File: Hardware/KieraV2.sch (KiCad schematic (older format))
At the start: 32 parts, among them J1 Conn_01x04_Male, J2 Conn_01x05_Male, SW3 SW_Push, SW4 SW_MEC_5G, SW5 SW_Push, SW6 SW_Push, U1 STM32L4P5RET6, Y1 Crystal_GND24

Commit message: added button for starting procedure, changes to pcb layout pending
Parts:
- removed C3, C5, C6: 100nF, Capacitor_SMD:C_0603_1608Metric, symbol Device:C
- removed R12, R14, R16: 1k, Resistor_SMD:R_0603_1608Metric, symbol Device:R
- removed R13, R15, R17: 10k, Resistor_SMD:R_0603_1608Metric, symbol Device:R
- removed SW3, SW5, SW6: SW_Push, Button_Switch_THT:MyPushbuttonSwitch, symbol Switch:SW_Push
- renumbered SW4 to SW7
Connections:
- net SW3: now also U1.51 (PC10)
- net SW4: now also U1.52 (PC11)
- net SW5: now also U1.53 (PC12)
- net SW6: now reaches U1.54 (PD2)
- no-connect marks 30 -> 29

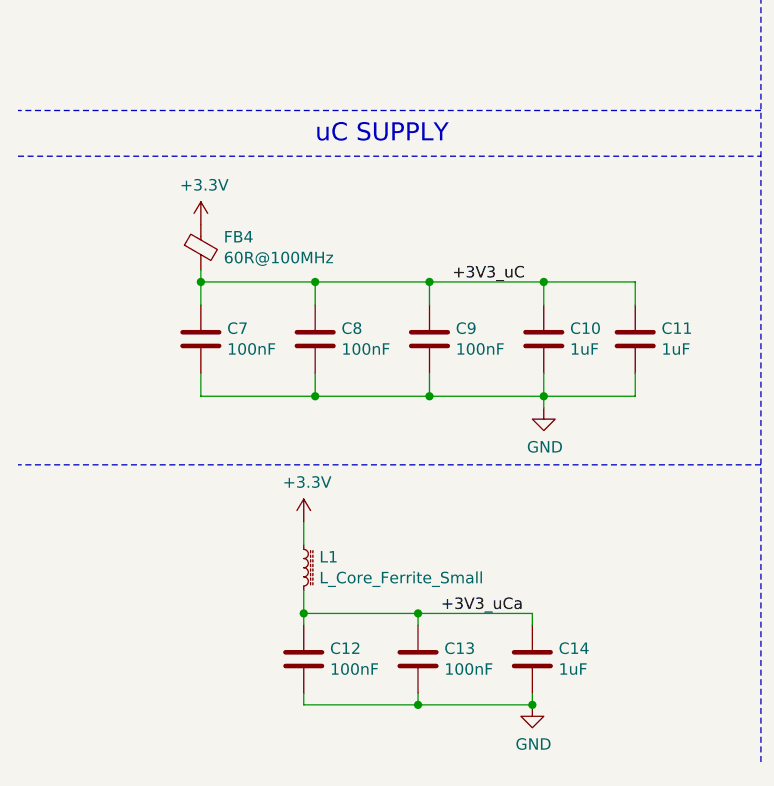
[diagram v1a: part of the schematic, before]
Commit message: controll leds are now groundend on uC, some changes of the pcb layout
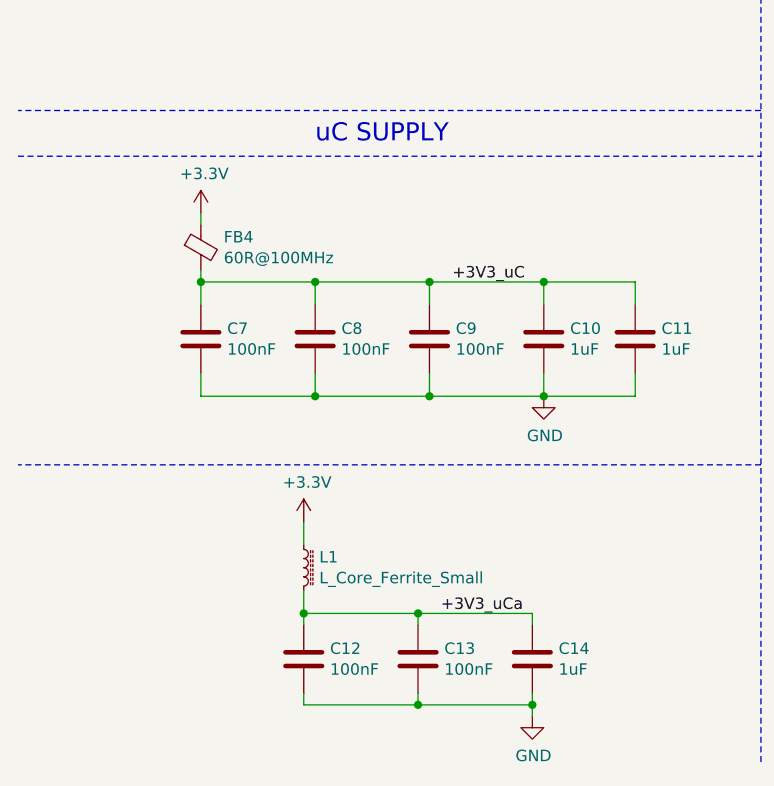
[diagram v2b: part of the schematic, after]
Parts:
- SW7: footprint Button_Switch_SMD:SW_Push_1P1T_NO_6x6mm_H9.5mm -> Button_Switch_SMD:SW_SPST_Omron_B3FS-100xP
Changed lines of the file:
@@
 	1    0    0    -1
 $EndComp
-$Comp
-L Device:C C7
-U 1 1 61B5E0FC
-P 1300 5900
-F 0 "C7" H 1415 5946 50  0000 L CNN
-F 1 "100nF" H 1415 5855 50  0000 L CNN
-F 2 "Capacitor_SMD:C_0603_1608Metric" H 1338 5750 50  0001 C CNN
-F 3 "~" H 1300 5900 50  0001 C CNN
-	1    1300 5900
-	1    0    0    -1
-$EndComp
-Wire Wire Line
-	1300 5650 1300 5750
-Wire Wire Line
-	1300 5650 1800 5650
-Wire Wire Line
-	1800 5650 1800 5750
-Wire Wire Line
-	1800 5650 2300 5650
-Wire Wire Line
-	2300 5650 2300 5750
-Connection ~ 1800 5650
-Wire Wire Line
-	2300 5650 2800 5650
-Connection ~ 2300 5650
-Wire Wire Line
-	1300 6050 1300 6150
 Wire Wire Line
 	1800 6050 1800 6150
@@
 L power:+3.3V #PWR014
 U 1 1 61B8345C
-P 1300 5400
-F 0 "#PWR014" H 1300 5250 50  0001 C CNN
-F 1 "+3.3V" H 1315 5573 50  0000 C CNN
-F 2 "" H 1300 5400 50  0001 C CNN
-F 3 "" H 1300 5400 50  0001 C CNN
-	1    1300 5400
+P 1300 5350
+F 0 "#PWR014" H 1300 5200 50  0001 C CNN
+F 1 "+3.3V" H 1315 5523 50  0000 C CNN
+F 2 "" H 1300 5350 50  0001 C CNN
+F 3 "" H 1300 5350 50  0001 C CNN
+	1    1300 5350
 	1    0    0    -1
 $EndComp
@@
 L power:GND #PWR017
 U 1 1 61B9E8D8
-P 2800 6200
-F 0 "#PWR017" H 2800 5950 50  0001 C CNN
-F 1 "GND" H 2805 6027 50  0000 C CNN
-F 2 "" H 2800 6200 50  0001 C CNN
-F 3 "" H 2800 6200 50  0001 C CNN
-	1    2800 6200
+P 2800 6150
+F 0 "#PWR017" H 2800 5900 50  0001 C CNN
+F 1 "GND" H 2805 5977 50  0000 C CNN
+F 2 "" H 2800 6150 50  0001 C CNN
+F 3 "" H 2800 6150 50  0001 C CNN
+	1    2800 6150
 	1    0    0    -1
 $EndComp
@@
 U 1 1 61DC36EF
 P 10200 2550
+AR Path="/61DC36EF" Ref="SW7"  Part="1"
+AR Path="/61B9B4C0/61DC36EF" Ref="SW7"  Part="1"
 F 0 "SW7" H 10200 2835 50  0000 C CNN
 F 1 "SW_MEC_5G" H 10200 2744 50  0000 C CNN
-F 2 "Button_Switch_SMD:SW_Push_1P1T_NO_6x6mm_H9.5mm" H 10200 2750 50  0001 C CNN
+F 2 "Button_Switch_SMD:SW_SPST_Omron_B3FS-100xP" H 10200 2750 50  0001 C CNN
 F 3 "http://www.apem.com/int/index.php?controller=attachment&id_attachment=488" H 10200 2750 50  0001 C CNN
 	1    10200 2550
@@
 Wire Notes Line
 	11200 3350 8600 3350
-Wire Wire Line
-	2800 5750 2800 5650
-$Comp
-L Device:C C10
-U 1 1 61A8C773
-P 2800 5900
-F 0 "C10" H 2915 5946 50  0000 L CNN
-F 1 "1uF" H 2915 5855 50  0000 L CNN
-F 2 "Capacitor_SMD:C_0603_1608Metric" H 2838 5750 50  0001 C CNN
-F 3 "~" H 2800 5900 50  0001 C CNN
-	1    2800 5900
-	1    0    0    -1
-$EndComp
 $Sheet
 S 8900 3750 1300 800
@@
 Text Label 5350 3550 0    50   ~ 0
 OSC_OUT
-Wire Wire Line
-	5350 3450 5850 3450
 Wire Wire Line
 	5350 3550 5850 3550
@@
 F1 "Power.sch" 50
 $EndSheet
-$Comp
-L Device:Ferrite_Bead_Small FB4
-U 1 1 61B5861E
-P 1300 5500
-F 0 "FB4" H 1400 5546 50  0000 L CNN
-F 1 "60R@100MHz" H 1400 5455 50  0000 L CNN
-F 2 "Inductor_SMD:L_0603_1608Metric" V 1230 5500 50  0001 C CNN
-F 3 "~" H 1300 5500 50  0001 C CNN
-	1    1300 5500
-	1    0    0    -1
-$EndComp
 Wire Wire Line
 	1800 6150 2300 6150
@@
 Connection ~ 2800 6150
 Wire Wire Line
-	2800 6200 2800 6150
-Wire Wire Line
 	2300 6150 2800 6150
 Wire Wire Line
 	2800 6150 2800 6050
-Wire Wire Line
-	1300 5600 1300 5650
-Connection ~ 1300 5650
 Text Label 2400 5650 0    50   ~ 0
 +3V3_uC
@@
 	3200 6150 2800 6150
 Wire Wire Line
-	2800 5650 3200 5650
-Wire Wire Line
 	3200 5650 3200 5750
-Connection ~ 2800 5650
 Wire Wire Line
 	10000 1400 10000 1350
@@
 L power:GND #PWR022
 U 1 1 61BA45BC
-P 2750 7500
-F 0 "#PWR022" H 2750 7250 50  0001 C CNN
-F 1 "GND" H 2755 7327 50  0000 C CNN
-F 2 "" H 2750 7500 50  0001 C CNN
-F 3 "" H 2750 7500 50  0001 C CNN
-	1    2750 7500
+P 2750 7550
+F 0 "#PWR022" H 2750 7300 50  0001 C CNN
+F 1 "GND" H 2755 7377 50  0000 C CNN
+F 2 "" H 2750 7550 50  0001 C CNN
+F 3 "" H 2750 7550 50  0001 C CNN
+	1    2750 7550
 	1    0    0    -1
 $EndComp
@@
 	2250 7100 2750 7100
 Wire Wire Line
-	1750 7100 1750 7150
-Connection ~ 1750 7100
-Wire Wire Line
 	1750 7100 2250 7100
 Wire Wire Line
@@
 Wire Wire Line
 	1750 7500 2250 7500
-Wire Wire Line
-	2750 7450 2750 7500
-Connection ~ 2750 7500
 Wire Wire Line
 	2250 7450 2250 7500
@@
 Wire Wire Line
 	1750 6700 1750 6800
-Wire Wire Line
-	1750 7000 1750 7100
 Text Label 2350 7100 0    50   ~ 0
 +3V3_uCa
@@
 Text Label 5350 5600 0    50   ~ 0
 SW5
+Wire Wire Line
+	2750 7550 2750 7500
+Connection ~ 2750 7500
+Wire Wire Line
+	2750 7500 2750 7450
+Wire Wire Line
+	1750 7000 1750 7100
+Connection ~ 1750 7100
+Wire Wire Line
+	1750 7100 1750 7150
+Wire Wire Line
+	1300 5350 1300 5400
+Wire Wire Line
+	1300 6050 1300 6150
+$Comp
+L Device:C C7
+U 1 1 61B5E0FC
+P 1300 5900
+F 0 "C7" H 1415 5946 50  0000 L CNN
+F 1 "100nF" H 1415 5855 50  0000 L CNN
+F 2 "Capacitor_SMD:C_0603_1608Metric" H 1338 5750 50  0001 C CNN
+F 3 "~" H 1300 5900 50  0001 C CNN
+	1    1300 5900
+	1    0    0    -1
+$EndComp
+$Comp
+L Device:Ferrite_Bead_Small FB4
+U 1 1 61B5861E
+P 1300 5500
+F 0 "FB4" H 1400 5546 50  0000 L CNN
+F 1 "60R@100MHz" H 1400 5455 50  0000 L CNN
+F 2 "Inductor_SMD:L_0603_1608Metric" V 1230 5500 50  0001 C CNN
+F 3 "~" H 1300 5500 50  0001 C CNN
+	1    1300 5500
+	1    0    0    -1
+$EndComp
+Wire Wire Line
+	1300 5750 1300 5650
+Wire Wire Line
+	1300 5650 1300 5600
+Connection ~ 1300 5650
+Wire Wire Line
+	2300 5650 2300 5750
+Connection ~ 2300 5650
+Wire Wire Line
+	2300 5650 2800 5650
+$Comp
+L Device:C C10
+U 1 1 61A8C773
+P 2800 5900
+F 0 "C10" H 2915 5946 50  0000 L CNN
+F 1 "1uF" H 2915 5855 50  0000 L CNN
+F 2 "Capacitor_SMD:C_0603_1608Metric" H 2838 5750 50  0001 C CNN
+F 3 "~" H 2800 5900 50  0001 C CNN
+	1    2800 5900
+	1    0    0    -1
+$EndComp
+Wire Wire Line
+	2800 5650 2800 5750
+Connection ~ 2800 5650
+Wire Wire Line
+	2800 5650 3200 5650
+Wire Wire Line
+	1300 5650 1800 5650
+Wire Wire Line
+	1800 5650 1800 5750
+Connection ~ 1800 5650
+Wire Wire Line
+	1800 5650 2300 5650
+Wire Wire Line
+	5350 3450 5850 3450
 $EndSCHEMATC

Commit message: power supply connector is now a micro-fit
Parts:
- J1: footprint Connector_PinHeader_2.54mm:PinHeader_1x04_P2.54mm_Vertical -> Connector_Molex:Molex_Micro-Fit_3.0_43650-0400_1x04_P3.00mm_Horizontal
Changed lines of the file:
@@
 F 0 "J1" H 1400 1000 50  0000 R CNN
 F 1 "Conn_01x04_Male" H 1400 900 50  0000 R CNN
-F 2 "Connector_PinHeader_2.54mm:PinHeader_1x04_P2.54mm_Vertical" H 1450 1000 50  0001 C CNN
+F 2 "Connector_Molex:Molex_Micro-Fit_3.0_43650-0400_1x04_P3.00mm_Horizontal" H 1450 1000 50  0001 C CNN
 F 3 "~" H 1450 1000 50  0001 C CNN
 	1    1450 1000

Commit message: new input 'connector', rearrangement
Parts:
- J1: footprint Connector_Molex:Molex_Micro-Fit_3.0_43650-0400_1x04_P3.00mm_Horizontal -> Connector_Wire:SolderWire-0.25sqmm_1x04_P4.2mm_D0.65mm_OD1.7mm_Relief
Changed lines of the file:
@@
 F 0 "J1" H 1400 1000 50  0000 R CNN
 F 1 "Conn_01x04_Male" H 1400 900 50  0000 R CNN
-F 2 "Connector_Molex:Molex_Micro-Fit_3.0_43650-0400_1x04_P3.00mm_Horizontal" H 1450 1000 50  0001 C CNN
+F 2 "Connector_Wire:SolderWire-0.25sqmm_1x04_P4.2mm_D0.65mm_OD1.7mm_Relief" H 1450 1000 50  0001 C CNN
 F 3 "~" H 1450 1000 50  0001 C CNN
 	1    1450 1000

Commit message: added 6pin connector and somme labels
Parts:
- J2: value Conn_01x05_Male -> Conn_01x06_Male; footprint Connector_PinHeader_2.54mm:PinHeader_1x05_P2.54mm_Vertical -> Connector_PinHeader_2.54mm:PinHeader_1x06_P2.54mm_Vertical; symbol Connector:Conn_01x05_Male -> Connector:Conn_01x06_Male
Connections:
- net SWO: now also J2.6 (Pin_6)
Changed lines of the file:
@@
 L power:GND #PWR04
 U 1 1 61A4CEAD
-P 7400 1150
-F 0 "#PWR04" H 7400 900 50  0001 C CNN
-F 1 "GND" H 7405 977 50  0000 C CNN
-F 2 "" H 7400 1150 50  0001 C CNN
-F 3 "" H 7400 1150 50  0001 C CNN
-	1    7400 1150
+P 7450 1050
+F 0 "#PWR04" H 7450 800 50  0001 C CNN
+F 1 "GND" H 7455 877 50  0000 C CNN
+F 2 "" H 7450 1050 50  0001 C CNN
+F 3 "" H 7450 1050 50  0001 C CNN
+	1    7450 1050
 	1    0    0    -1
 $EndComp
@@
 $EndComp
 $Comp
-L Connector:Conn_01x05_Male J2
+L Connector:Conn_01x06_Male J2
 U 1 1 61ACE4C5
-P 6650 1150
-F 0 "J2" H 6550 1200 50  0000 C CNN
-F 1 "Conn_01x05_Male" H 6250 1100 50  0000 C CNN
-F 2 "Connector_PinHeader_2.54mm:PinHeader_1x05_P2.54mm_Vertical" H 6650 1150 50  0001 C CIN
-F 3 "~" H 6650 1150 50  0001 C CNN
-	1    6650 1150
-	1    0    0    -1
-$EndComp
-Wire Wire Line
-	7400 1150 6850 1150
-Wire Wire Line
-	7400 950  6850 950
+P 6700 1050
+F 0 "J2" H 6600 1100 50  0000 C CNN
+F 1 "Conn_01x06_Male" H 6300 1000 50  0000 C CNN
+F 2 "Connector_PinHeader_2.54mm:PinHeader_1x06_P2.54mm_Vertical" H 6700 1050 50  0001 C CIN
+F 3 "~" H 6700 1050 50  0001 C CNN
+	1    6700 1050
+	1    0    0    -1
+$EndComp
+Wire Wire Line
+	7450 1050 6900 1050
+Wire Wire Line
+	7450 850  6900 850
 Text Notes 5900 700  0    79   ~ 0
 SWD
@@
 L power:+3.3V #PWR03
 U 1 1 61B51C6E
-P 7400 900
-F 0 "#PWR03" H 7400 750 50  0001 C CNN
-F 1 "+3.3V" H 7415 1073 50  0000 C CNN
-F 2 "" H 7400 900 50  0001 C CNN
-F 3 "" H 7400 900 50  0001 C CNN
-	1    7400 900
+P 7450 800
+F 0 "#PWR03" H 7450 650 50  0001 C CNN
+F 1 "+3.3V" H 7465 973 50  0000 C CNN
+F 2 "" H 7450 800 50  0001 C CNN
+F 3 "" H 7450 800 50  0001 C CNN
+	1    7450 800
 	1    0    0    -1
 $EndComp
@@
 CAN_TX
 Wire Wire Line
-	7400 950  7400 900
+	7450 850  7450 800
 Connection ~ 9200 850
 Connection ~ 9200 1350
@@
 Text Label 2000 1100 2    50   ~ 0
 CAN-
-Text Label 7250 1050 2    50   ~ 0
+Text Label 7300 950  2    50   ~ 0
 SWCLK
-Text Label 7250 1350 2    50   ~ 0
+Text Label 7300 1250 2    50   ~ 0
 NRST
-Text Label 7250 1250 2    50   ~ 0
+Text Label 7300 1150 2    50   ~ 0
 SWDIO
 Wire Wire Line
-	6850 1050 7250 1050
-Wire Wire Line
-	6850 1250 7250 1250
-Wire Wire Line
-	6850 1350 7250 1350
+	6900 950  7300 950
+Wire Wire Line
+	6900 1150 7300 1150
+Wire Wire Line
+	6900 1250 7300 1250
 Text Label 2000 1000 2    50   ~ 0
 CAN+
@@
 Wire Wire Line
 	5350 3450 5850 3450
+Wire Wire Line
+	7300 1350 6900 1350
+Text Label 7300 1350 2    50   ~ 0
+SWO
 $EndSCHEMATC
